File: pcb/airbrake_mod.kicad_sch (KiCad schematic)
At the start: 3 parts

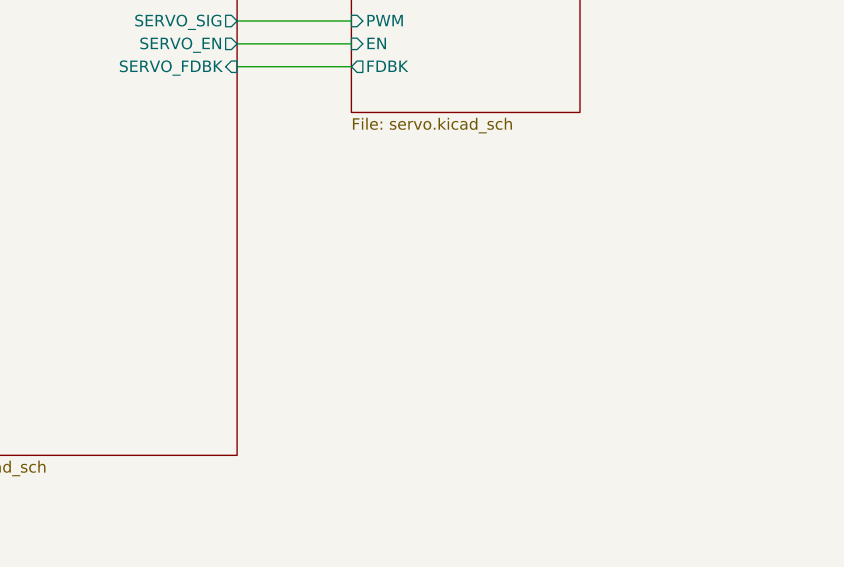
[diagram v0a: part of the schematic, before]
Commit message: Add production files for quoting
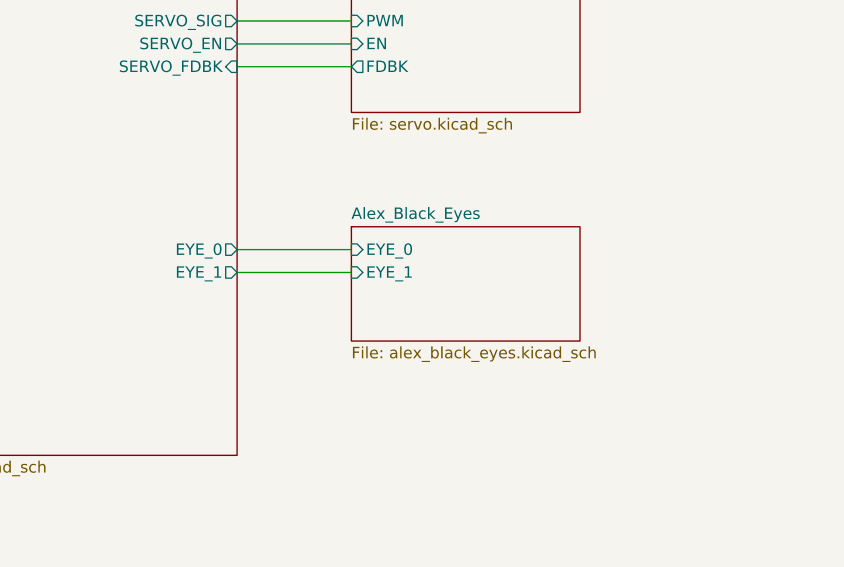
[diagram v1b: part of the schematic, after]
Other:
- added sheet Alex_Black_Eyes (alex_black_eyes.kicad_sch)
- sheet MCU ports: added EYE_0, EYE_1; removed none
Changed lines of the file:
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@@
+	(wire
+		(pts
+			(xy 101.6 144.78) (xy 114.3 144.78)
+		)
+		(stroke
+			(width 0)
+			(type default)
+		)
+	)
 	(wire
 		(pts
@@
 		(pts
 			(xy 101.6 41.91) (xy 114.3 41.91)
+		)
+		(stroke
+			(width 0)
+			(type default)
+		)
+	)
+	(wire
+		(pts
+			(xy 101.6 142.24) (xy 114.3 142.24)
 		)
 		(stroke
@@
 			)
 		)
+		(pin "EYE_0" output
+			(at 101.6 142.24 0)
+			(effects
+				(font
+					(size 1.27 1.27)
+				)
+				(justify right)
+			)
+		)
+		(pin "EYE_1" output
+			(at 101.6 144.78 0)
+			(effects
+				(font
+					(size 1.27 1.27)
+				)
+				(justify right)
+			)
+		)
 		(instances
 			(project "airbrake_mod"
@@
 				)
 			)
+		)
+	)
+	(sheet
+		(at 114.3 139.7)
+		(size 25.4 12.7)
+		(exclude_from_sim no)
+		(in_bom yes)
+		(on_board yes)
+		(dnp no)
+		(fields_autoplaced yes)
+		(stroke
+			(width 0.1524)
+			(type solid)
+		)
+		(fill
+			(color 255 255 194 1.0000)
+		)
+		(property "Sheetname" "Alex_Black_Eyes"
+			(at 114.3 138.9884 0)
+			(effects
+				(font
+					(size 1.27 1.27)
+				)
+				(justify left bottom)
+			)
+		)
+		(property "Sheetfile" "alex_black_eyes.kicad_sch"
+			(at 114.3 152.9846 0)
+			(effects
+				(font
+					(size 1.27 1.27)
+				)
+				(justify left top)
+			)
+		)
+		(pin "EYE_1" input
+			(at 114.3 144.78 180)
+			(effects
+				(font
+					(size 1.27 1.27)
+				)
+				(justify left)
+			)
+		)
+		(pin "EYE_0" input
+			(at 114.3 142.24 180)
+			(effects
+				(font
+					(size 1.27 1.27)
+				)
+				(justify left)
+			)
+		)
+		(instances
+			(project "airbrake_mod"
+				(path "/1f4fd4ed-9886-4375-a5ac-dc32d5760936"
+					(page "10")
+				)
+			)

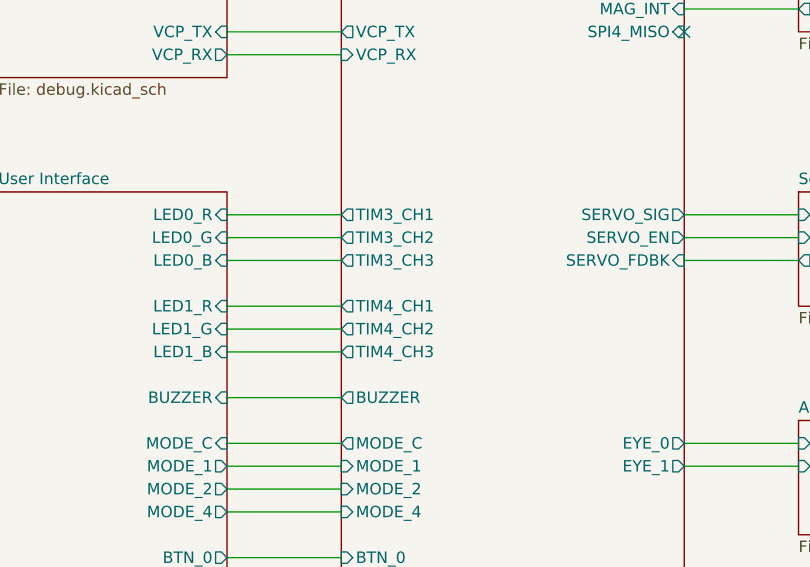
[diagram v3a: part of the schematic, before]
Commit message: Improve baro routing
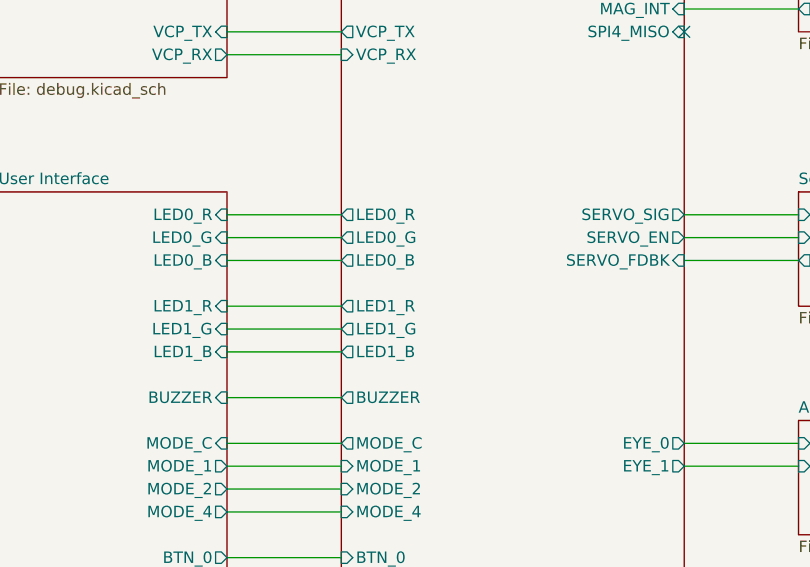
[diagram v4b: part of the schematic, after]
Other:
- sheet MCU ports: added LED0_B, LED0_G, LED0_R, LED1_B, LED1_G, LED1_R; removed TIM3_CH1, TIM3_CH2, TIM3_CH3, TIM4_CH1, TIM4_CH2, TIM4_CH3
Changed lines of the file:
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@@
-			)
-		)
-		(pin "TIM3_CH3" output
-			(at 63.5 121.92 180)
-			(effects
-				(font
-					(size 1.27 1.27)
-				)
-				(justify left)
-			)
-		)
-		(pin "TIM3_CH1" output
-			(at 63.5 116.84 180)
-			(effects
-				(font
-					(size 1.27 1.27)
-				)
-				(justify left)
-			)
-		)
-		(pin "TIM3_CH2" output
-			(at 63.5 119.38 180)
-			(effects
-				(font
-					(size 1.27 1.27)
-				)
-				(justify left)
 			)
 		)
@@
 			)
 		)
-		(pin "TIM4_CH2" output
-			(at 63.5 129.54 180)
-			(effects
-				(font
-					(size 1.27 1.27)
-				)
-				(justify left)
-			)
-		)
-		(pin "TIM4_CH3" output
-			(at 63.5 132.08 180)
-			(effects
-				(font
-					(size 1.27 1.27)
-				)
-				(justify left)
-			)
-		)
-		(pin "TIM4_CH1" output
-			(at 63.5 127 180)
-			(effects
-				(font
-					(size 1.27 1.27)
-				)
-				(justify left)
-			)
-		)
 		(pin "MODE_1" input
 			(at 63.5 144.78 180)
@@
 			)
 		)
+		(pin "LED0_R" output
+			(at 63.5 116.84 180)
+			(effects
+				(font
+					(size 1.27 1.27)
+				)
+				(justify left)
+			)
+		)
+		(pin "LED0_B" output
+			(at 63.5 121.92 180)
+			(effects
+				(font
+					(size 1.27 1.27)
+				)
+				(justify left)
+			)
+		)
+		(pin "LED1_G" output
+			(at 63.5 129.54 180)
+			(effects
+				(font
+					(size 1.27 1.27)
+				)
+				(justify left)
+			)
+		)
+		(pin "LED1_R" output
+			(at 63.5 127 180)
+			(effects
+				(font
+					(size 1.27 1.27)
+				)
+				(justify left)
+			)
+		)
+		(pin "LED0_G" output
+			(at 63.5 119.38 180)
+			(effects
+				(font
+					(size 1.27 1.27)
+				)
+				(justify left)
+			)
+		)
+		(pin "LED1_B" output
+			(at 63.5 132.08 180)
+			(effects
+				(font
+					(size 1.27 1.27)
+				)
+				(justify left)
+			)
+		)
